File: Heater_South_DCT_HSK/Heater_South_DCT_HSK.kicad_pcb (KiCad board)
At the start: 2 copper layers, 53.3 x 57.1 mm, 5 parts, among them J1 South_Heater_1, J2 South_Heater_2, J3 Internal_Heater_DCT_HSK_Box

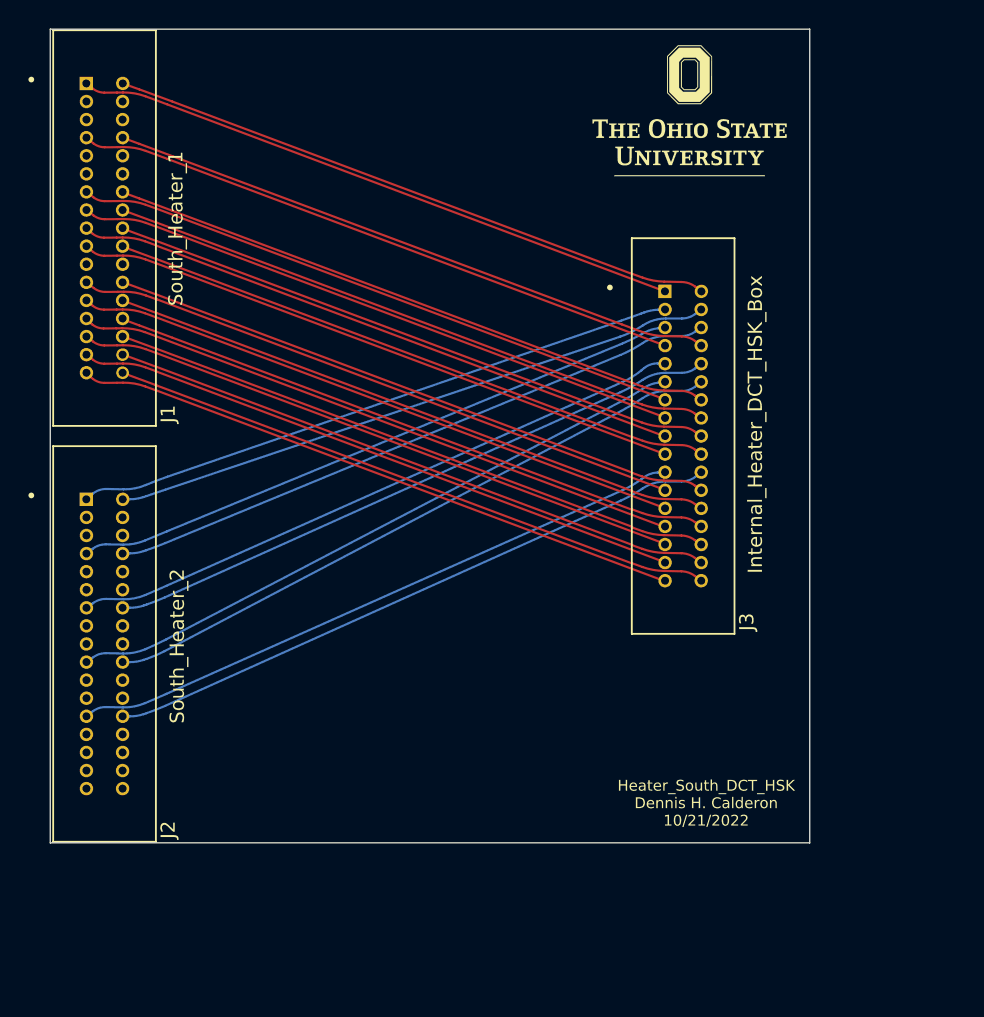
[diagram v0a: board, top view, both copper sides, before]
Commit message: Updated Heater and Temp PCBs to board size 2.5in x 2.1in. Updated traces and silkscreens
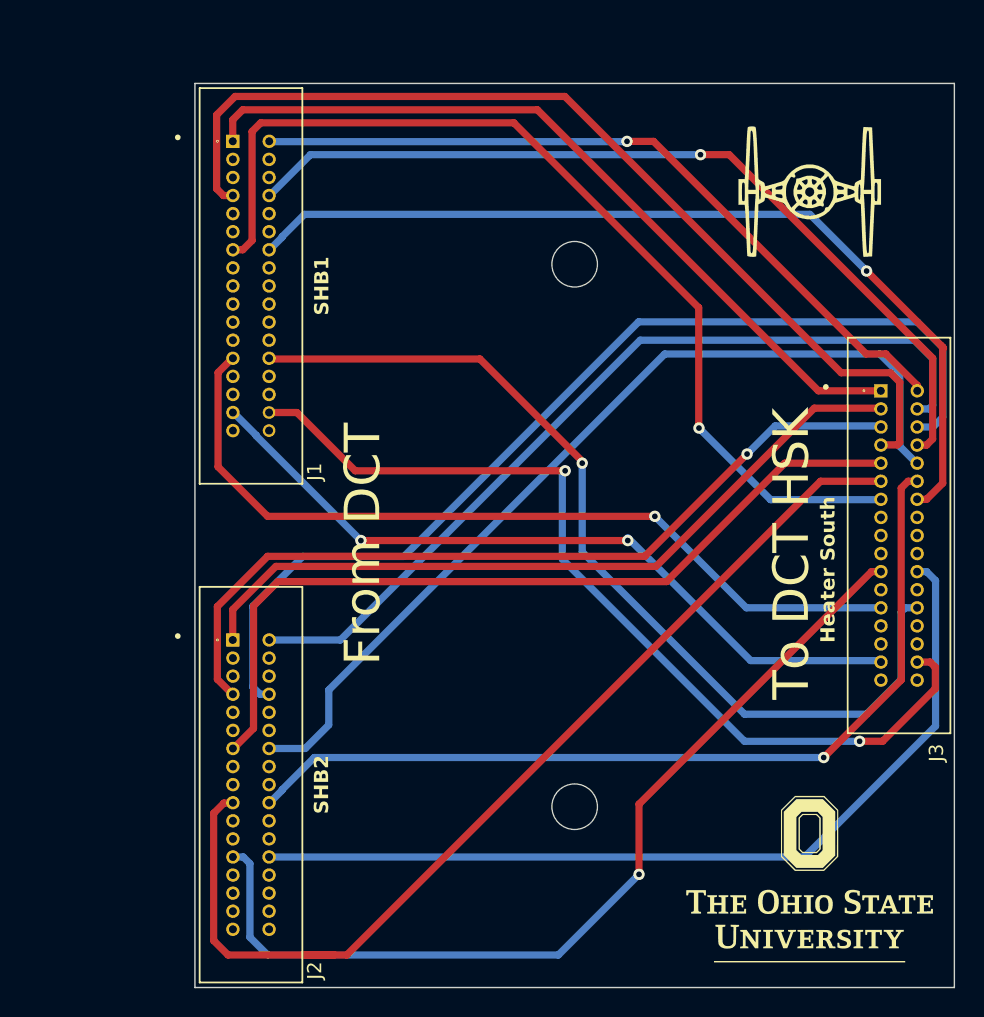
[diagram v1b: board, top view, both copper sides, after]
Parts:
- removed the G*** at (136.3, 52.7)
- removed the G*** at (125.2, 76.1)
- added G***: Tie Fighter, Fun_Logos:Tie Fighter, F.Cu at (144.8, 58.4)
- added G***: Medium OSU, Fun_Logos:Medium OSU, F.Cu at (144.8, 106.7)
- added G***: , Fun_Logos:Super Large OSU, B.Cu at (139.0, 82.5)
- added REF**: H1, MountingHole:MountingHole_3.2mm_M3_DIN965, F.Cu at (128.3, 63.5)
- added REF**: H2, MountingHole:MountingHole_3.2mm_M3_DIN965, F.Cu at (128.3, 101.6)
- J1: value South_Heater_1 -> SHB1
- J2: value South_Heater_2 -> SHB2
- J3: value Internal_Heater_DCT_HSK_Box -> Heater South
- moved J3 16.7 mm to (151.1, 82.5)
- moved J2 14.3 mm to (105.5, 100.1)
- moved J1 11.1 mm to (105.5, 65.0)
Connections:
- net /HB_1 renamed /HB1_1
- net /HB_10 renamed /HB2_14
- net /HB_11 renamed /HB2_19
- net /HB_12 renamed /HB2_20
- net /HB_13 renamed /HB1_13
- net /HB_14 renamed /HB1_14
- net /HB_2 renamed /HB1_2
- net /HB_21 renamed /HB2_25
- net /HB_22 renamed /HB2_26
- net /HB_25 renamed /HB1_25
- net /HB_26 renamed /HB1_26
- net /HB_3 renamed /HB2_1
- net /HB_31 renamed /HB1_31
- net /HB_32 renamed /HB1_32
- net /HB_4 renamed /HB2_2
- net /HB_5 renamed /HB2_7
- net /HB_6 renamed /HB2_8
- net /HB_7 renamed /HB1_7
- net /HB_8 renamed /HB1_8
- net /HB_9 renamed /HB2_13
- J1 pad 15: /HB_15 -> unconnected-(J1-Pin_15-Pad15)
- J1 pad 16: /HB_16 -> unconnected-(J1-Pin_16-Pad16)
- J1 pad 17: /HB_17 -> unconnected-(J1-Pin_17-Pad17)
- J1 pad 18: /HB_18 -> unconnected-(J1-Pin_18-Pad18)
- J1 pad 19: /HB_19 -> unconnected-(J1-Pin_19-Pad19)
- J1 pad 20: /HB_20 -> unconnected-(J1-Pin_20-Pad20)
- J1 pad 23: /HB_23 -> unconnected-(J1-Pin_23-Pad23)
- J1 pad 24: /HB_24 -> unconnected-(J1-Pin_24-Pad24)
- J1 pad 27: /HB_27 -> unconnected-(J1-Pin_27-Pad27)
- J1 pad 28: /HB_28 -> unconnected-(J1-Pin_28-Pad28)
- J1 pad 29: /HB_29 -> unconnected-(J1-Pin_29-Pad29)
- J1 pad 30: /HB_30 -> unconnected-(J1-Pin_30-Pad30)
- J1 pad 33: /HB_33 -> unconnected-(J1-Pin_33-Pad33)
- J1 pad 34: /HB_34 -> unconnected-(J1-Pin_34-Pad34)
- J3 pad 15: /HB_15 -> unconnected-(J3-Pin_15-Pad15)
- J3 pad 16: /HB_16 -> unconnected-(J3-Pin_16-Pad16)
- J3 pad 17: /HB_17 -> unconnected-(J3-Pin_17-Pad17)
- J3 pad 18: /HB_18 -> unconnected-(J3-Pin_18-Pad18)
- J3 pad 19: /HB_19 -> unconnected-(J3-Pin_19-Pad19)
- J3 pad 20: /HB_20 -> unconnected-(J3-Pin_20-Pad20)
- J3 pad 23: /HB_23 -> unconnected-(J3-Pin_23-Pad23)
- J3 pad 24: /HB_24 -> unconnected-(J3-Pin_24-Pad24)
- J3 pad 27: /HB_27 -> unconnected-(J3-Pin_27-Pad27)
- J3 pad 28: /HB_28 -> unconnected-(J3-Pin_28-Pad28)
- J3 pad 29: /HB_29 -> unconnected-(J3-Pin_29-Pad29)
- J3 pad 30: /HB_30 -> unconnected-(J3-Pin_30-Pad30)
- J3 pad 33: /HB_33 -> unconnected-(J3-Pin_33-Pad33)
- J3 pad 34: /HB_34 -> unconnected-(J3-Pin_34-Pad34)
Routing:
- net /HB_24: track 43.3 -> 0.00 mm
- net /HB_30: track 43.3 -> 0.00 mm
- net /HB_16: track 43.3 -> 0.00 mm
- net /HB_34: track 43.3 -> 0.00 mm
- net /HB_18: track 43.3 -> 0.00 mm
- net /HB_20: track 43.3 -> 0.00 mm
- net /HB_28: track 43.3 -> 0.00 mm
- net /HB_23: track 43.3 -> 0.00 mm
- net /HB_15: track 43.3 -> 0.00 mm
- net /HB_27: track 43.3 -> 0.00 mm
- net /HB_17: track 43.3 -> 0.00 mm
- net /HB_33: track 43.3 -> 0.00 mm
- net /HB_19: track 43.3 -> 0.00 mm
- net /HB_29: track 43.3 -> 0.00 mm
- net /HB2_19: track 45.4 -> 73.8 mm
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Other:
- board size 53.3 x 57.1 mm -> 53.3 x 63.5 mm
- board text added: "From DCT"
- board text added: "Heater South Rev B Dennis H. Calderon 09/09/2023"
- board text added: "South"
- board text added: "To DCT HSK"
- board text removed: "Heater_South_DCT_HSK Dennis H. Calderon 10/21/2022"
